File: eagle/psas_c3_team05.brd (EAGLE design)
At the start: 76.2 x 71.1 mm, 96 parts, among them IC1 CP2102, J1 3220-10-0100-00, J2 1.27MM_HDR_2X12X1, U1 MIC5319 3.3V, U2 MCP73871, U3 MKW01Z128, X1 32 MHz

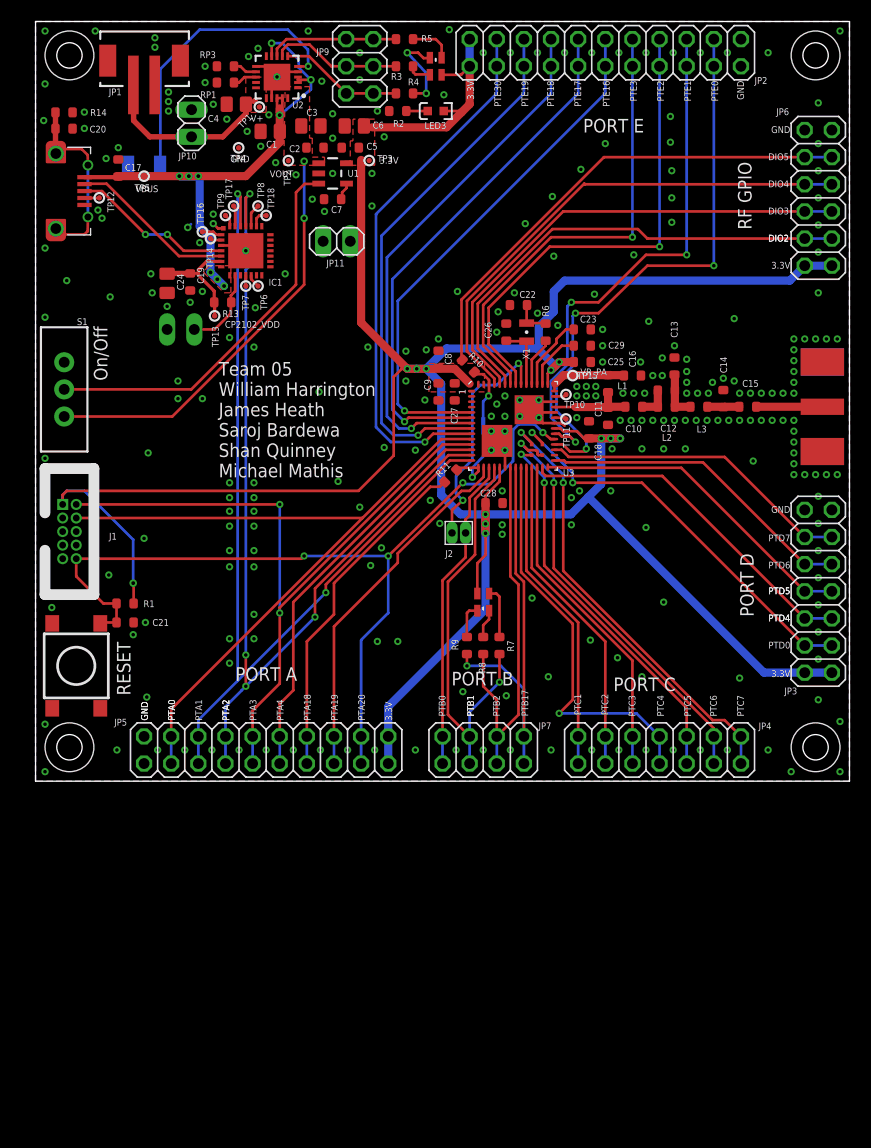
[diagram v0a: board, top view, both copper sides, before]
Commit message: Adding the last RF component values
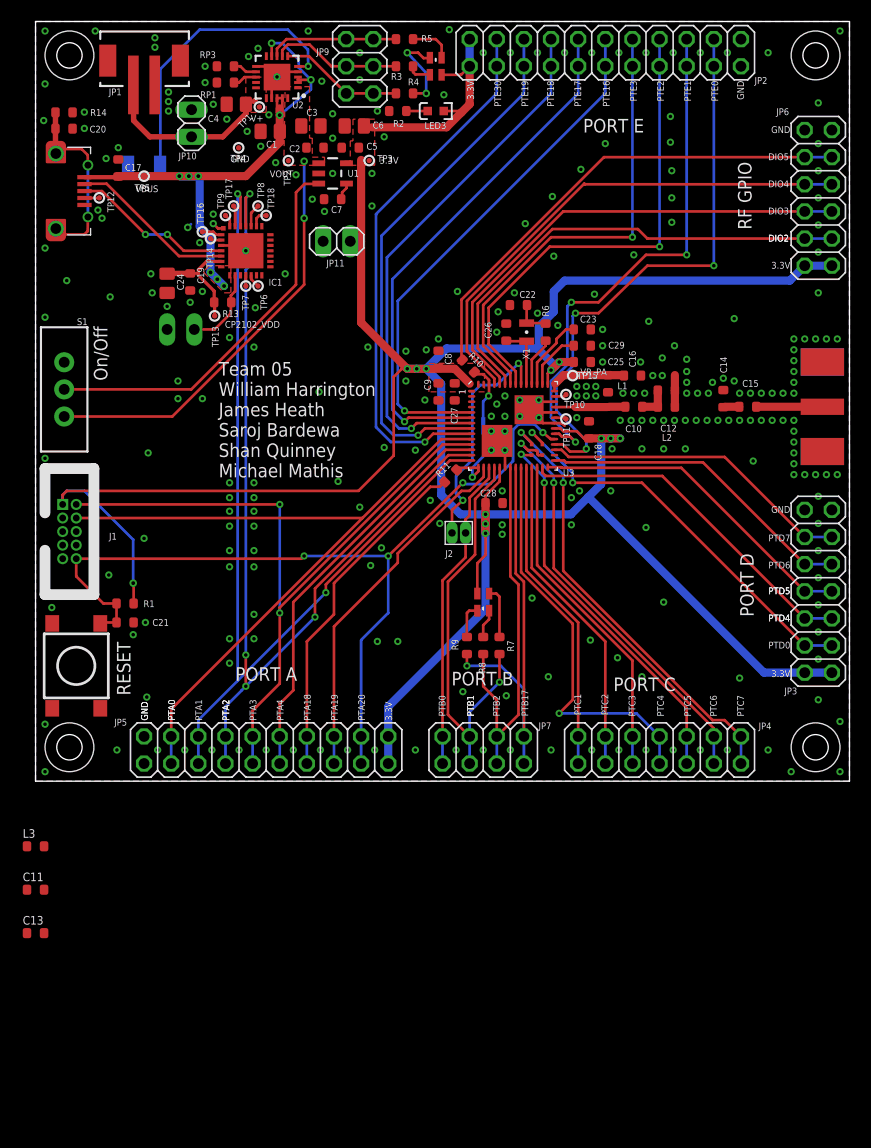
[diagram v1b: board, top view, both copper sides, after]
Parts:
- moved C13 80.0 mm to (0.00, -14.2), turned to 0 degrees
- moved L3 74.5 mm to (0.00, -6.10)
- moved C11 69.5 mm to (0.00, -10.2), turned to 0 degrees
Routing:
- net RFIO: track 8.14 -> 6.48 mm
- net N$21: track 3.44 -> 1.83 mm
- net N$17: track 4.47 -> 2.97 mm

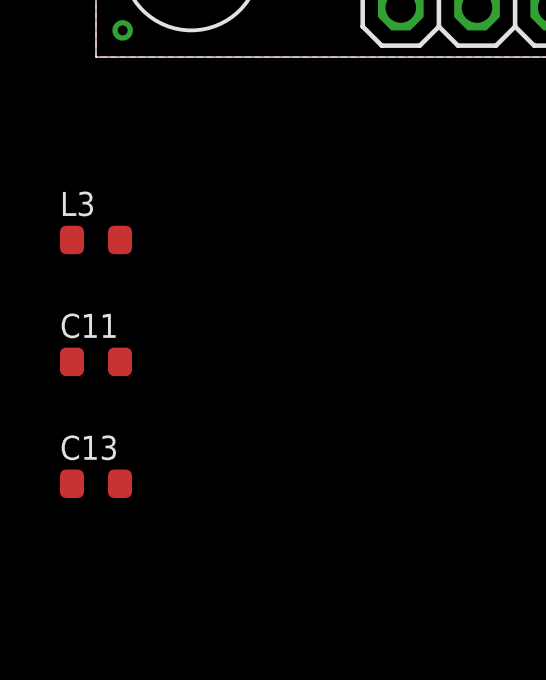
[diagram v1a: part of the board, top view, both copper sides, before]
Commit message: Added final part attrib RF
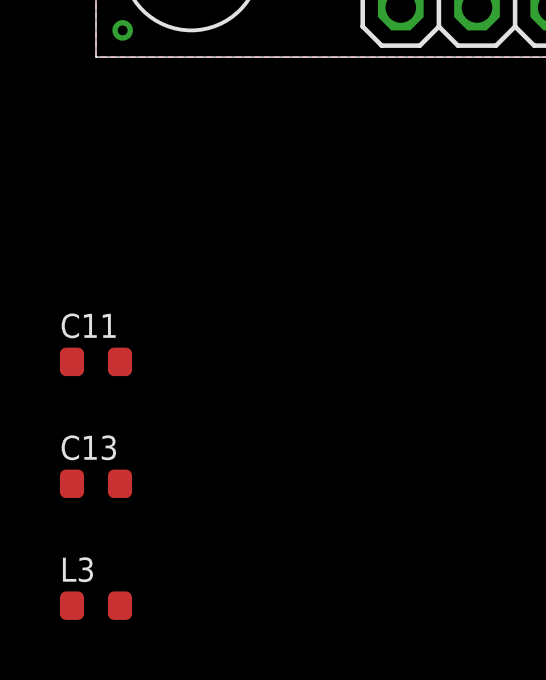
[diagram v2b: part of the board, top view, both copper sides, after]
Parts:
- moved L3 12.2 mm to (0.00, -18.3)
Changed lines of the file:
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@@
 <attribute name="VALUE" x="66.7196" y="36.119" size="0.8128" layer="27" font="vector" ratio="15"/>
 <attribute name="NAME" x="66.675" y="35.052" size="0.3" layer="33" ratio="15" align="center"/>
-<attribute name="DPN" value="490-1532-1-ND" x="66.675" y="35.052" size="1.778" layer="27" display="off"/>
+<attribute name="DPN" value="478-5778-1-ND" x="66.675" y="35.052" size="1.778" layer="27" display="off"/>
+<attribute name="DIST" value="Digi-Key" x="66.675" y="35.052" size="1.778" layer="27" display="off"/>
+<attribute name="MFG" value="AVX" x="66.675" y="35.052" size="1.778" layer="27" display="off"/>
+<attribute name="MFG-PN" value="06035C104JAT2A" x="66.675" y="35.052" size="1.778" layer="27" display="off"/>
 </element>
 <element name="C16" library="rcl_custom" package=".0603-B-NOSILK" value="10nF" x="55.88" y="37.973" smashed="yes" rot="R180">
@@
 <attribute name="VALUE" x="56.8514" y="36.8298" size="0.8128" layer="27" font="vector" ratio="15" rot="R180"/>
 <attribute name="NAME" x="55.88" y="37.973" size="0.3" layer="33" ratio="15" rot="R180" align="center"/>
+<attribute name="DIST" value="Digi-Key" x="55.88" y="37.973" size="1.778" layer="27" rot="R180" display="off"/>
+<attribute name="DPN" value="478-6208-1-ND" x="55.88" y="37.973" size="1.778" layer="27" rot="R180" display="off"/>
+<attribute name="MFG" value="AVX" x="55.88" y="37.973" size="1.778" layer="27" rot="R180" display="off"/>
+<attribute name="MFG-PN" value="0603YC103JAT2A" x="55.88" y="37.973" size="1.778" layer="27" rot="R180" display="off"/>
 </element>
 <element name="C2" library="rcl_custom" package=".0603-B-NOSILK" value="100nF" x="26.162" y="59.309" smashed="yes">
@@
 <attribute name="VALUE" x="54.4324" y="38.6142" size="0.8128" layer="27" font="vector" ratio="15" rot="R270"/>
 <attribute name="NAME" x="53.594" y="37.211" size="0.3" layer="33" ratio="15" rot="R270" align="center"/>
+<attribute name="DIST" value="Digi-Key" x="53.594" y="37.211" size="1.778" layer="27" rot="R270" display="off"/>
+<attribute name="DPN" value="490-6874-1-ND" x="53.594" y="37.211" size="1.778" layer="27" rot="R270" display="off"/>
+<attribute name="MFG" value="Murata" x="53.594" y="37.211" size="1.778" layer="27" rot="R270" display="off"/>
+<attribute name="MFG-PN" value="LQW18AN22NG00D" x="53.594" y="37.211" size="1.778" layer="27" rot="R270" display="off"/>
 </element>
 <element name="L2" library="rcl_custom" package=".0603-B-NOSILK" value="15n" x="59.055" y="35.052" smashed="yes">
@@
 <attribute name="VALUE" x="58.7186" y="33.6298" size="0.8128" layer="27" font="vector" ratio="15"/>
 <attribute name="NAME" x="59.055" y="35.052" size="0.3" layer="33" ratio="15" align="center"/>
+<attribute name="DIST" value="Digi-Key" x="59.055" y="35.052" size="1.778" layer="27" display="off"/>
+<attribute name="DPN" value="490-6866-1-ND" x="59.055" y="35.052" size="1.778" layer="27" display="off"/>
+<attribute name="MFG" value="Murata" x="59.055" y="35.052" size="1.778" layer="27" display="off"/>
+<attribute name="MFG-PN" value="LQW18AN15NG00D" x="59.055" y="35.052" size="1.778" layer="27" display="off"/>
 </element>
 <element name="RP1" library="rcl_custom" package=".0603-B-NOSILK" value="5k" x="17.78" y="65.405" smashed="yes">
@@
 <attribute name="NAME" x="37.719" y="36.449" size="0.3" layer="33" ratio="15" rot="R270" align="center"/>
 </element>
-<element name="U$2" library="SMAJ16-ND" package="SMAJ716-ND" value="SMAJ716-ND" x="73.152" y="35.052" smashed="yes" rot="R270"/>
+<element name="U$2" library="SMAJ16-ND" package="SMAJ716-ND" value="SMAJ716-ND" x="73.152" y="35.052" smashed="yes" rot="R270">
+<attribute name="DIST" value="Digi-Key" x="73.152" y="35.052" size="1.778" layer="27" rot="R270" display="off"/>
+<attribute name="DPN" value="J716-ND" x="73.152" y="35.052" size="1.778" layer="27" rot="R270" display="off"/>
+<attribute name="MFG" value="Cinch Connectivity Solutions" x="73.152" y="35.052" size="1.778" layer="27" rot="R270" display="off"/>
+<attribute name="MFG-PN" value="142-0701-806" x="73.152" y="35.052" size="1.778" layer="27" rot="R270" display="off"/>
+</element>
 <element name="TP6" library="microbuilder" package="TESTPOINT_ROUND_0.5MM" value="" x="20.828" y="46.355" smashed="yes" rot="R90">
 <attribute name="NAME" x="21.68653125" y="44.12488125" size="0.635" layer="25" font="vector" ratio="20" rot="R90"/>
@@
 <attribute name="VALUE" x="30.734" y="53.721" size="1.27" layer="27" rot="R180"/>
 </element>
-<element name="L3" library="rcl_custom" package=".0603-B-NOSILK" value="15n" x="0" y="-6.096"/>
 <element name="C11" library="rcl_custom" package=".0603-B-NOSILK" value="12p" x="0" y="-10.16">
 <attribute name="MFG" value="AVX" x="0" y="-10.16" size="1.778" layer="27" display="off"/>
@@
 <attribute name="MFG-PN" value="06031A150FAT2A" x="0" y="-14.224" size="1.778" layer="27" display="off"/>
 <attribute name="DPN" value="478-6024-1-ND" x="0" y="-14.224" size="1.778" layer="27" display="off"/>
+</element>
+<element name="L3" library="rcl_custom" package=".0603-B-NOSILK" value="15n" x="0" y="-18.288">
+<attribute name="DPN" value="490-6866-1-ND" x="0" y="-18.288" size="1.778" layer="27" display="off"/>
+<attribute name="MFG-PN" value="LQW18AN15NG00D" x="0" y="-18.288" size="1.778" layer="27" display="off"/>
+<attribute name="MFG" value="Murata" x="0" y="-18.288" size="1.778" layer="27" display="off"/>
+<attribute name="DIST" value="Digi-Key" x="0" y="-18.288" size="1.778" layer="27" display="off"/>
 </element>
 </elements>
@@
 <wire x1="59.855" y1="36.576" x2="59.855" y2="35.052" width="0.762" layer="1"/>
 <wire x1="59.855" y1="36.576" x2="59.855" y2="38.024" width="0.762" layer="1"/>
+<contactref element="C13" pad="1"/>
 <contactref element="L3" pad="1"/>
-<contactref element="C13" pad="1"/>
-<wire x1="-0.8" y1="-6.096" x2="59.855" y2="35.052" width="0" layer="19" extent="1-1"/>
-<wire x1="-0.8" y1="-14.224" x2="-0.8" y2="-6.096" width="0" layer="19" extent="1-1"/>
+<wire x1="-0.8" y1="-14.224" x2="59.855" y2="35.052" width="0" layer="19" extent="1-1"/>
+<wire x1="-0.8" y1="-18.288" x2="-0.8" y2="-14.224" width="0" layer="19" extent="1-1"/>
 </signal>
 <signal name="N$18">
@@
 <wire x1="64.3" y1="34.925" x2="64.389" y2="35.014" width="0.254" layer="1"/>
 <contactref element="L3" pad="2"/>
-<wire x1="0.8" y1="-6.096" x2="64.262" y2="34.925" width="0" layer="19" extent="1-1"/>
+<wire x1="0.8" y1="-18.288" x2="64.262" y2="34.925" width="0" layer="19" extent="1-1"/>
 </signal>
 <signal name="PTA1">

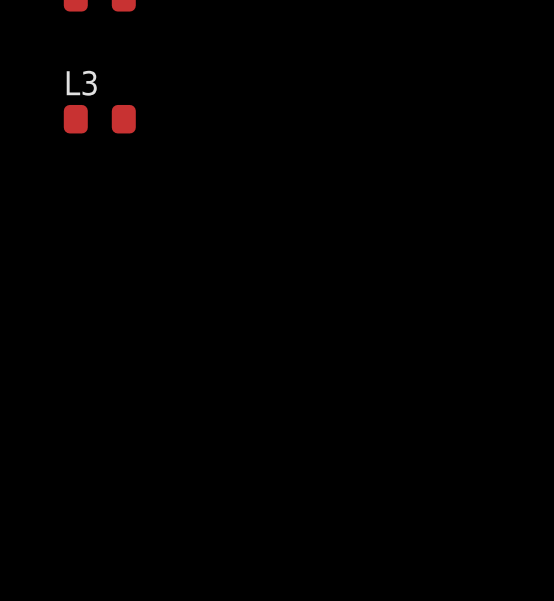
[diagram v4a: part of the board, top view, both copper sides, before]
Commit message: added more attributes for part numbers, duplicated crystal because crystal footprint is wrong on the board and we will need to order two just in case things go wrong with the first, hopefully one of the two work lol
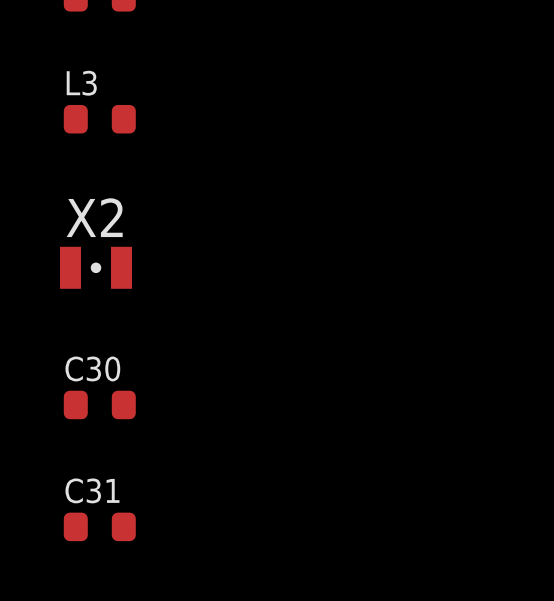
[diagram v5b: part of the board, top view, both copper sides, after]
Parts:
- added C30, C31: 5pF, Vibrogait_prototype:.0603-B-NOSILK
- added X2: 32 MHz, crystal:FC-12M
- C22, C26: value 11pF -> 4pF
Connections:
- new net N$14: C31.1, X2.2
- new net N$16: C30.1, X2.1
- net GND: now also C30.2, C31.2
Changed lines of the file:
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@@
 <attribute name="MFG" value="AVX Corp/Kyocera Corp" x="45.974" y="42.037" size="1.778" layer="27" rot="R90" display="off"/>
 <attribute name="MFG-PN" value="CX3225GA32000D0PTVCC" x="45.974" y="42.037" size="1.778" layer="27" rot="R90" display="off"/>
-<attribute name="DPN2" value="CTX1364CT-ND" x="45.974" y="42.037" size="1.778" layer="27" rot="R90" display="off"/>
-<attribute name="MFG2" value="CTS-Frequency Controls" x="45.974" y="42.037" size="1.778" layer="27" rot="R90" display="off"/>
-<attribute name="MFG2-PN" value="402F3201XIAR" x="45.974" y="42.037" size="1.778" layer="27" rot="R90" display="off"/>
 </element>
 <element name="R6" library="rcl_custom" package=".0603-B-NOSILK" value="0" x="47.752" y="42.037" smashed="yes" rot="R270">
@@
 <attribute name="NAME" x="47.9806" y="42.1386" size="0.3" layer="33" ratio="15" rot="R270" align="center"/>
 </element>
-<element name="C22" library="Vibrogait_prototype" package=".0603-B-NOSILK" value="11pF" x="45.212" y="44.577" smashed="yes" rot="R180">
-<attribute name="MPN" value="GRM188R71C104KA01D" x="45.212" y="44.577" size="1.778" layer="27" rot="R180" display="off"/>
-<attribute name="DPN" value="490-1532-1-ND" x="45.212" y="44.577" size="1.778" layer="27" rot="R180" display="off"/>
+<element name="C22" library="Vibrogait_prototype" package=".0603-B-NOSILK" value="4pF" x="45.212" y="44.577" smashed="yes" rot="R180">
+<attribute name="MPN" value="GRM1885C1H4R0CA01D" x="45.212" y="44.577" size="1.778" layer="27" rot="R180" display="off"/>
+<attribute name="DPN" value="490-10720-6-ND" x="45.212" y="44.577" size="1.778" layer="27" rot="R180" display="off"/>
 <attribute name="DIST" value="Digi-Key" x="45.212" y="44.577" size="1.778" layer="27" rot="R180" display="off"/>
 <attribute name="MFG" value="Murata Electronics North America" x="45.212" y="44.577" size="1.778" layer="27" rot="R180" display="off"/>
@@
 <attribute name="NAME" x="45.1866" y="44.577" size="0.3" layer="33" ratio="15" rot="R180" align="center"/>
 </element>
-<element name="C26" library="Vibrogait_prototype" package=".0603-B-NOSILK" value="11pF" x="44.069" y="42.037" smashed="yes" rot="R90">
-<attribute name="MPN" value="GRM188R71C104KA01D" x="44.069" y="42.037" size="1.778" layer="27" rot="R90" display="off"/>
-<attribute name="DPN" value="490-1532-1-ND" x="44.069" y="42.037" size="1.778" layer="27" rot="R90" display="off"/>
+<element name="C26" library="Vibrogait_prototype" package=".0603-B-NOSILK" value="4pF" x="44.069" y="42.037" smashed="yes" rot="R90">
+<attribute name="MPN" value="GRM1885C1H4R0CA01D" x="44.069" y="42.037" size="1.778" layer="27" rot="R90" display="off"/>
+<attribute name="DPN" value="490-10720-6-ND" x="44.069" y="42.037" size="1.778" layer="27" rot="R90" display="off"/>
 <attribute name="DIST" value="Digi-Key" x="44.069" y="42.037" size="1.778" layer="27" rot="R90" display="off"/>
 <attribute name="MFG" value="Murata Electronics North America" x="44.069" y="42.037" size="1.778" layer="27" rot="R90" display="off"/>
@@
 <attribute name="MFG" value="Murata" x="0" y="-18.288" size="1.778" layer="27" display="off"/>
 <attribute name="DIST" value="Digi-Key" x="0" y="-18.288" size="1.778" layer="27" display="off"/>
+</element>
+<element name="X2" library="crystal" package="FC-12M" value="32 MHz" x="-0.127" y="-23.241">
+<attribute name="DIST" value="Digi-Key" x="-0.127" y="-23.241" size="1.778" layer="27" display="off"/>
+<attribute name="MFG" value="CTS-Frequency Controls" x="-0.127" y="-23.241" size="1.778" layer="27" display="off"/>
+<attribute name="MFG-PN" value="402F3201XIAR" x="-0.127" y="-23.241" size="1.778" layer="27" display="off"/>
+<attribute name="DPN" value="CTX1364CT-ND" x="-0.127" y="-23.241" size="1.778" layer="27" display="off"/>
+</element>
+<element name="C30" library="Vibrogait_prototype" package=".0603-B-NOSILK" value="5pF" x="0" y="-27.813">
+<attribute name="DPN" value="490-10720-6-ND" x="0" y="-27.813" size="1.778" layer="27" display="off"/>
+<attribute name="MFG" value="Murata Electronics North America" x="0" y="-27.813" size="1.778" layer="27" display="off"/>
+<attribute name="DIST" value="Digi-Key" x="0" y="-27.813" size="1.778" layer="27" display="off"/>
+<attribute name="MPN" value="GRM1885C1H4R0CA01D" x="0" y="-27.813" size="1.778" layer="27" display="off"/>
+</element>
+<element name="C31" library="Vibrogait_prototype" package=".0603-B-NOSILK" value="5pF" x="0" y="-31.877">
+<attribute name="DPN" value="490-10720-6-ND" x="0" y="-31.877" size="1.778" layer="27" display="off"/>
+<attribute name="MFG" value="Murata Electronics North America" x="0" y="-31.877" size="1.778" layer="27" display="off"/>
+<attribute name="DIST" value="Digi-Key" x="0" y="-31.877" size="1.778" layer="27" display="off"/>
+<attribute name="MPN" value="GRM1885C1H4R0CA01D" x="0" y="-31.877" size="1.778" layer="27" display="off"/>
 </element>
 </elements>
@@
 <contactref element="C11" pad="2"/>
 <contactref element="C13" pad="2"/>
+<contactref element="C31" pad="2"/>
+<contactref element="C30" pad="2"/>
 <wire x1="73.279" y1="63.5" x2="75.311" y2="70.231" width="0" layer="19" extent="1-1"/>
 <wire x1="74.549" y1="60.96" x2="73.279" y2="63.5" width="0" layer="19" extent="1-1"/>
@@
 <wire x1="0.8" y1="-10.16" x2="0.889" y2="0.889" width="0" layer="19" extent="1-1"/>
 <wire x1="0.8" y1="-14.224" x2="0.8" y2="-10.16" width="0" layer="19" extent="1-1"/>
+<wire x1="0.8" y1="-27.813" x2="0.8" y2="-14.224" width="0" layer="19" extent="1-1"/>
+<wire x1="0.8" y1="-31.877" x2="0.8" y2="-27.813" width="0" layer="19" extent="1-1"/>
 </signal>
 <signal name="VOUT">
@@
 <wire x1="25.4" y1="13.081" x2="25.4" y2="4.191" width="0.254" layer="1"/>
 </signal>
+<signal name="N$14">
+<contactref element="C31" pad="1"/>
+<contactref element="X2" pad="2"/>
+<wire x1="0.723" y1="-23.241" x2="-0.8" y2="-31.877" width="0" layer="19" extent="1-1"/>
+</signal>
+<signal name="N$16">
+<contactref element="C30" pad="1"/>
+<contactref element="X2" pad="1"/>
+<wire x1="-0.977" y1="-23.241" x2="-0.8" y2="-27.813" width="0" layer="19" extent="1-1"/>
+</signal>
 </signals>
